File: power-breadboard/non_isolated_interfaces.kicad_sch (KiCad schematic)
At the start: 28 parts, among them J1 Network Connector, J2 Screw_Terminal_01x02, U1 TPS5430DDA, U4 SN65HVD230

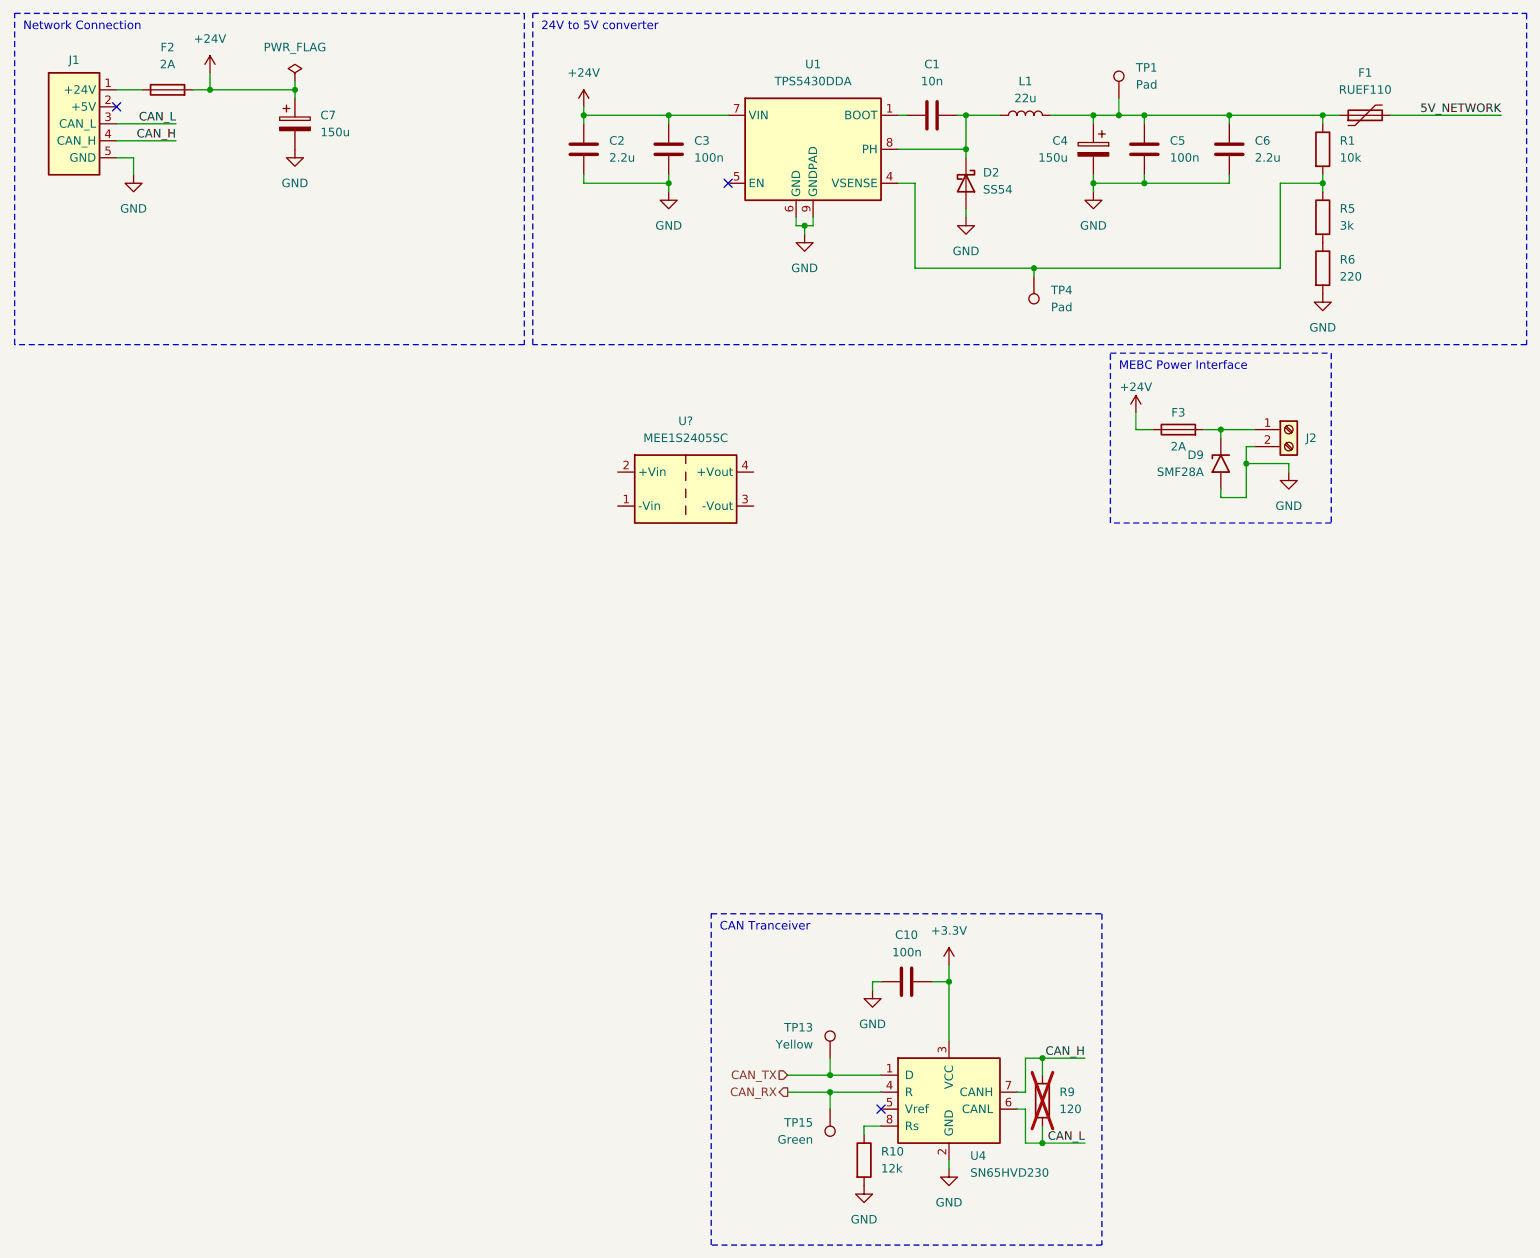
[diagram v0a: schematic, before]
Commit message: power-breadboard: complete non-iso. interfaces
- CAN transceiver
- Power input (battery and 24V->5V converter)
- MEBC telemetry power connector
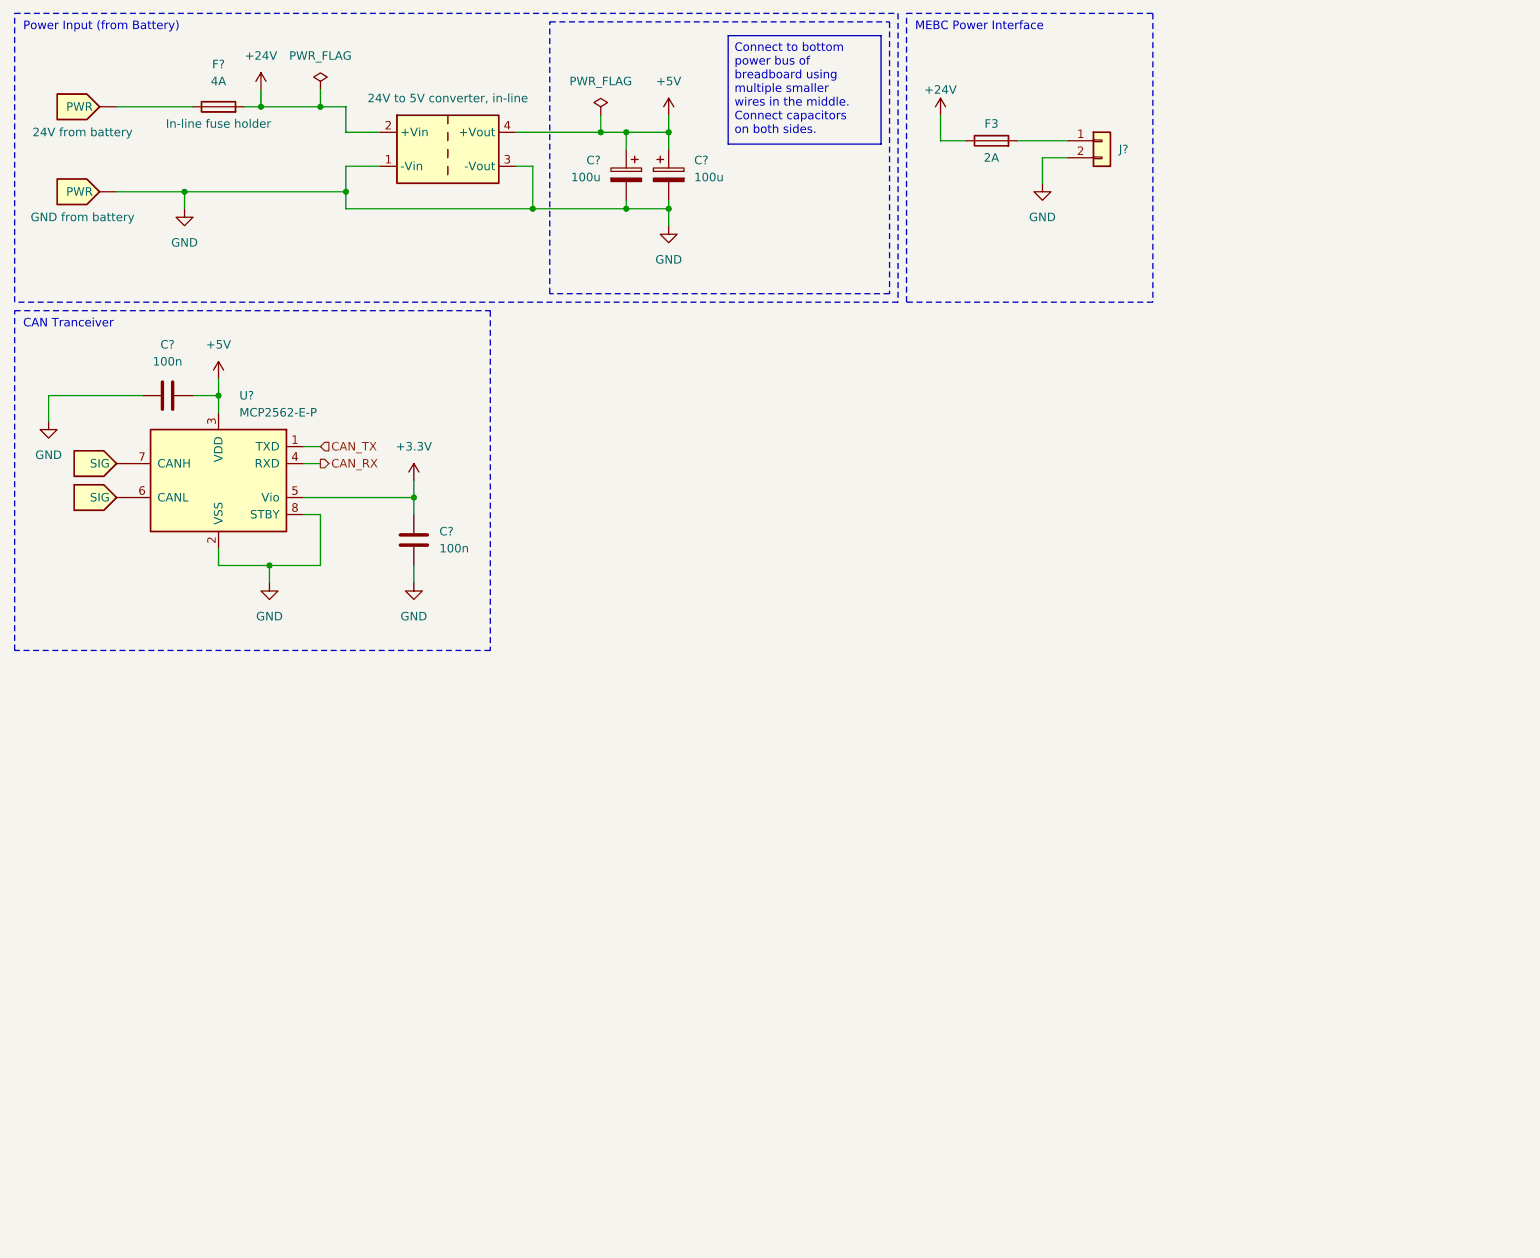
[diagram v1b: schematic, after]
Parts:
- removed C1: 10n, Capacitor_SMD:C_0402_1005Metric_Pad0.74x0.62mm_HandSolder, symbol Device:C
- removed C10, C3, C5: 100n, Capacitor_SMD:C_0402_1005Metric_Pad0.74x0.62mm_HandSolder, symbol Device:C
- removed C2, C6: 2.2u, Capacitor_SMD:C_0805_2012Metric_Pad1.18x1.45mm_HandSolder, symbol Device:C
- removed C4, C7: 150u, Capacitor_THT:CP_Radial_D8.0mm_P3.50mm, symbol Device:C_Polarized
- removed D2: SS54, Diode_SMD:D_SMA_Handsoldering, symbol Device:D_Schottky
- removed D9: SMF28A, Diode_SMD:D_SMF, symbol Diode:SMF28A
- removed F1: RUEF110, Fuse:Fuse_Littelfuse_395Series, symbol Device:Polyfuse
- removed F2: 2A, Exocet:Fuseholder_Littelfuse_Combined, symbol Device:Fuse
- removed J1: Network Connector, Connector_Molex:Molex_SPOX_5268-05A_1x05_P2.50mm_Horizontal, symbol Exocet:Network_Connector
- removed J2: Screw_Terminal_01x02, Exocet:Wuerth_Term_Blk_2pos_Side_Entry_5mm, symbol Connector:Screw_Terminal_01x02
- removed L1: 22u, Inductor_THT:L_Axial_L16.0mm_D6.3mm_P5.08mm_Vertical_Fastron_VHBCC, symbol Device:L
- removed R1: 10k, Resistor_SMD:R_0805_2012Metric_Pad1.20x1.40mm_HandSolder, symbol Device:R
- removed R10: 12k, Resistor_SMD:R_0402_1005Metric_Pad0.72x0.64mm_HandSolder, symbol Device:R
- removed R5: 3k, Resistor_SMD:R_0603_1608Metric_Pad0.98x0.95mm_HandSolder, symbol Device:R
- removed R6: 220, Resistor_SMD:R_0402_1005Metric_Pad0.72x0.64mm_HandSolder, symbol Device:R
- removed R9: 120, Resistor_THT:R_Axial_DIN0309_L9.0mm_D3.2mm_P12.70mm_Horizontal, symbol Device:R
- removed TP1, TP4: Pad, TestPoint:TestPoint_Pad_D1.5mm, symbol Connector:TestPoint
- removed TP13: Yellow, TestPoint:TestPoint_Keystone_5005-5009_Compact, symbol Connector:TestPoint
- removed TP15: Green, TestPoint:TestPoint_Keystone_5005-5009_Compact, symbol Connector:TestPoint
- removed U1: TPS5430DDA, Package_SO:TI_SO-PowerPAD-8_ThermalVias, symbol Regulator_Switching:TPS5430DDA
- removed U4: SN65HVD230, Package_SO:SOIC-8_3.9x4.9mm_P1.27mm, symbol Interface_CAN_LIN:SN65HVD230
- added C? (x2): 100u, symbol Device:C_Polarized
- added C? (x2): 100n, symbol Device:C
- added F?: 4A, Exocet:Fuseholder_Littelfuse_Combined, symbol Device:Fuse
- added J?: Conn_01x02, symbol Connector_Generic:Conn_01x02
- added U?: MCP2562-E-P, Package_DIP:DIP-8_W7.62mm, symbol Interface_CAN_LIN:MCP2562-E-P
- U?: value MEE1S2405SC -> (none); footprint Converter_DCDC:Converter_DCDC_Murata_MEE1SxxxxSC_THT -> (none)
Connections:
- net +24V: now also U?.2 (+Vin), F?.2
- net +3.3V: now also C?.1, U?.5 (Vio)
- net CAN_RX: now also U?.4 (RXD)
- net CAN_TX: now also U?.1 (TXD)
- net GND: now also U?.1 (-Vin), U?.3 (-Vout), C?.1, C?.2, C?.2, C?.2, J?.2 (Pin_2), U?.2 (VSS), U?.8 (STBY)
- net at F3.2: now also J?.1 (Pin_1)
- net +5V: now reaches U?.4 (+Vout)
- net +5V: now also C?.1, C?.1, C?.2, U?.3 (VDD)
- no-connect marks 3 -> 0
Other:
- note added: "Power Input (from Battery)"
- note removed: "24V to 5V converter"
- note removed: "Network Connection"
- moved on the sheet: F3

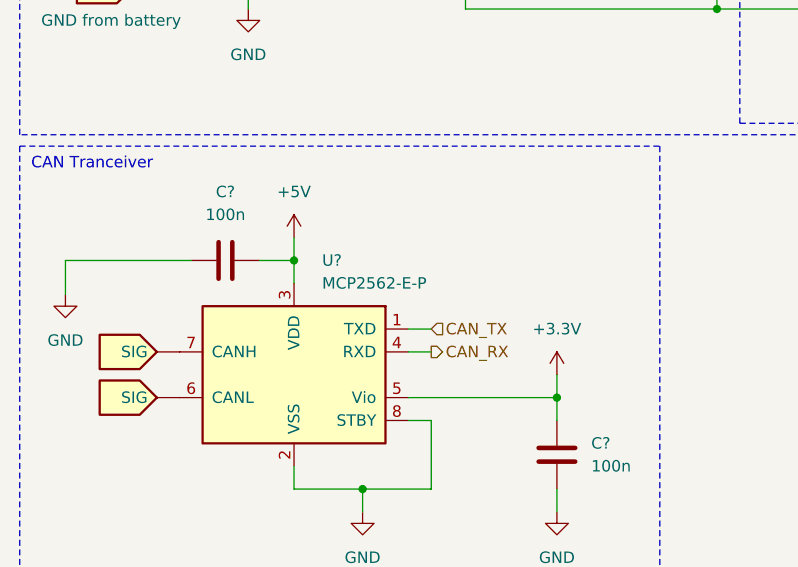
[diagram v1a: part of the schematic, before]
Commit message: power-breadboard: add nucleo pinout connections
- Replace the schematic page with STM32 microcontroller connections.
- Update the date on all pages and some page names
- Add CN10/CN7 connectors, with the CN7 being connected through the
  T-cobbler
- Add peripheral assignation table
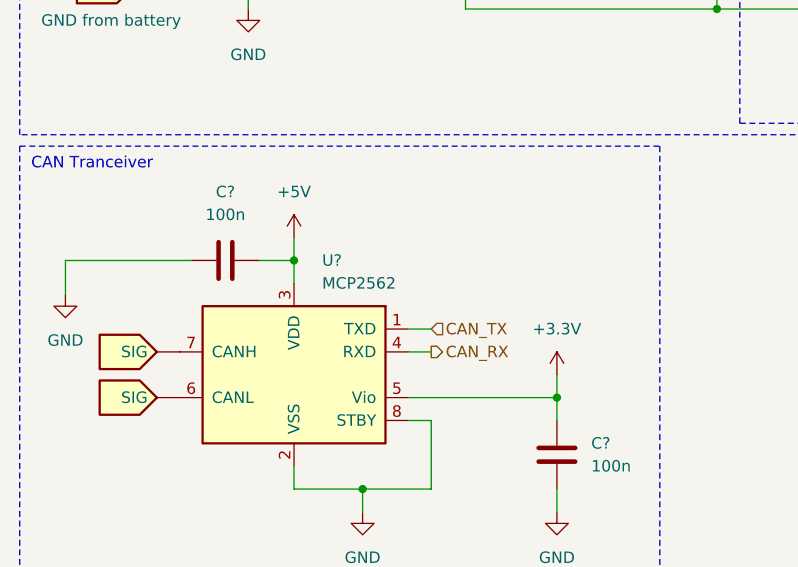
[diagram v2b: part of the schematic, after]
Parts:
- U?: value MCP2562-E-P -> MCP2562
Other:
- title: Non-Isolated Interfaces and Power -> Power Input and CAN
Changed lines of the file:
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@@
 	(paper "A4")
 	(title_block
-		(title "Non-Isolated Interfaces and Power")
-		(date "2026-06-19")
+		(title "Power Input and CAN")
+		(date "2026-06-29")
 		(rev "v1.1.0")
 	)
@@
 			)
 		)
-		(property "Value" "MCP2562-E-P"
+		(property "Value" "MCP2562"
 			(at 46.2981 72.39 0)
 			(show_name no)

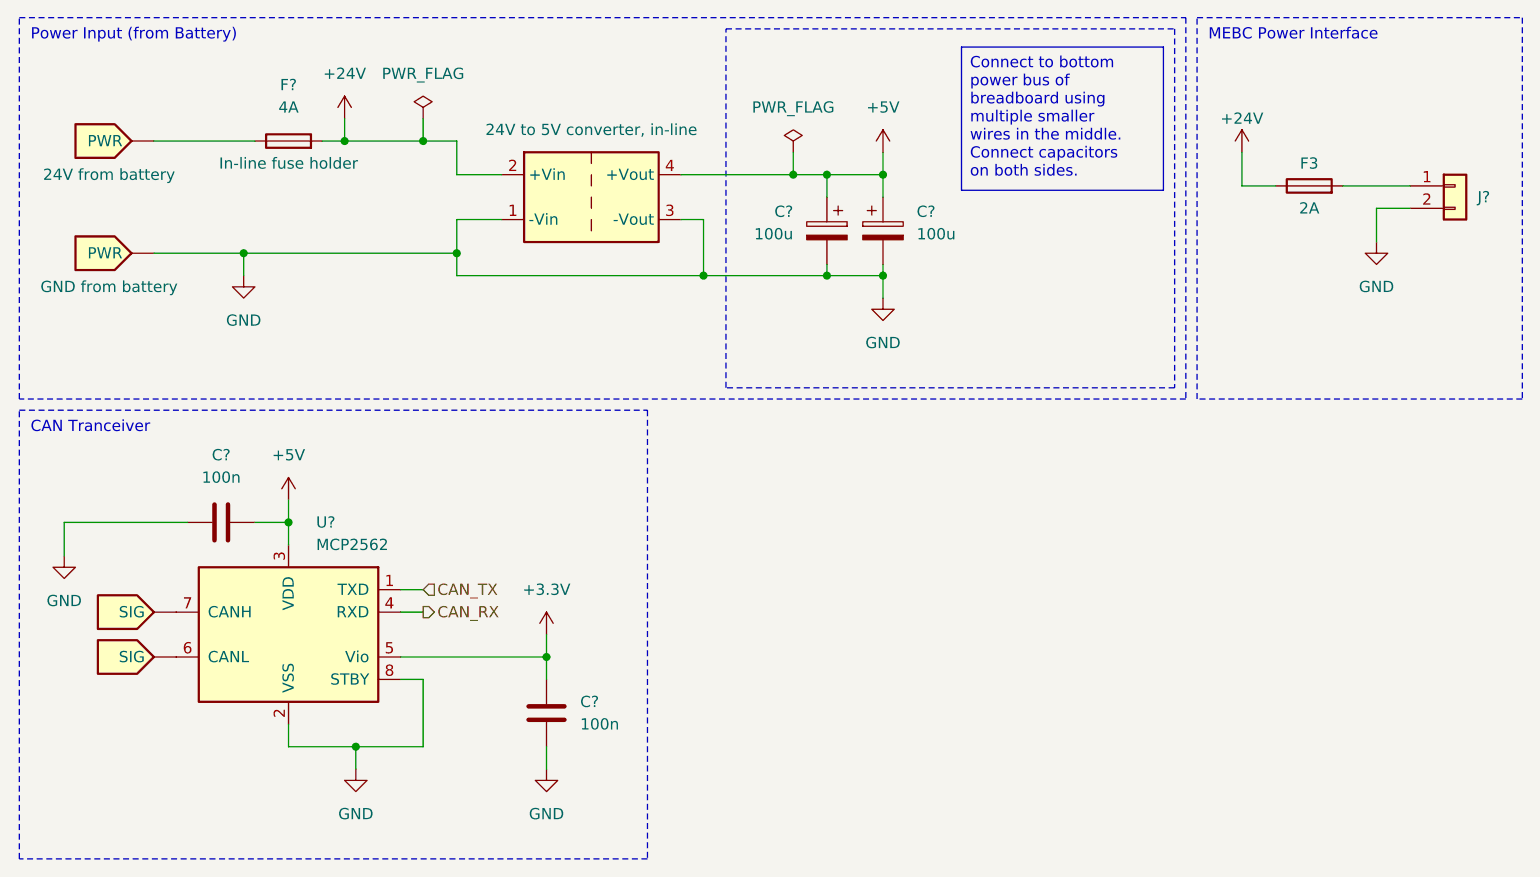
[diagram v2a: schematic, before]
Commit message: power-breadboard: use RECOM for 24V->5V conv.
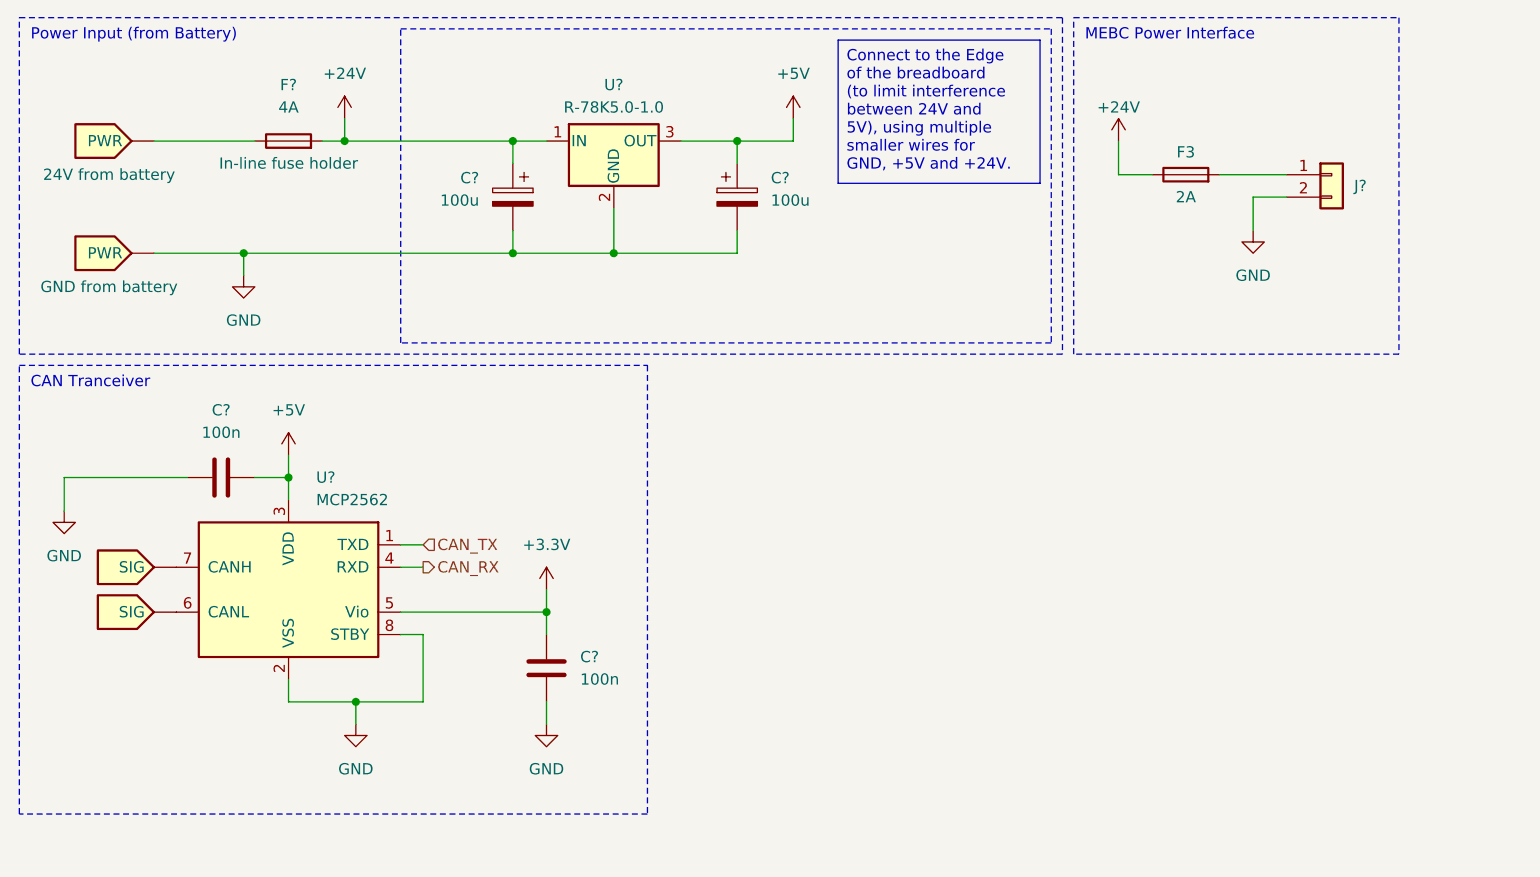
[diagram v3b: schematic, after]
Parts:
- removed C?: 100u, symbol Device:C_Polarized
- removed U?: (no value), symbol Converter_DCDC:MEE1S2405SC
- added C?: 100u, symbol Device:C_Polarized
- added U?: R-78K5.0-1.0, Converter_DCDC:Converter_DCDC_RECOM_R-78B-2.0_THT, symbol Converter_DCDC:R-78B5.0-2.0
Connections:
- net +24V: now also C?.1, U?.1 (IN)
- net +5V: now also U?.3 (OUT)
- net GND: now also C?.2, U?.2 (GND)
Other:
- moved on the sheet: C?, F3, J?, U?
